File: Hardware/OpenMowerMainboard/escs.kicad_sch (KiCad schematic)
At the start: 3 parts, among them U4 xESC2, U5 xESC2, U6 xESC2

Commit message: wip schematic
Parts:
- added D10, D11, D12, D4, D5, D6, D7, D8, D9: D_TVS, Diode_SMD:D_SMB, symbol Device:D_TVS
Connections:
- net MC_HALL_U: now also D7.2 (A2), D9.2 (A2)
- net MC_HALL_V: now also D7.1 (A1), D8.2 (A2)
- net MC_HALL_W: now also D8.1 (A1), D9.1 (A1)
- net ML_HALL_U: now also D4.2 (A2), D6.2 (A2)
- net ML_HALL_V: now also D4.1 (A1), D5.2 (A2)
- net ML_HALL_W: now also D5.1 (A1), D6.1 (A1)
- net MR_HALL_U: now also D10.2 (A2), D12.2 (A2)
- net MR_HALL_V: now also D10.1 (A1), D11.2 (A2)
- net MR_HALL_W: now also D11.1 (A1), D12.1 (A1)

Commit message: wip
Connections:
- net MC_HALL_U: no longer D7.2 (A2), D9.2 (A2)
- net MC_HALL_V: no longer D7.1 (A1), D8.2 (A2)
- net MC_HALL_W: no longer D8.1 (A1), D9.1 (A1)
- net MC_PHASE_U: now also D7.2 (A2), D9.2 (A2)
- net MC_PHASE_V: now also D7.1 (A1), D8.2 (A2)
- net MC_PHASE_W: now also D8.1 (A1), D9.1 (A1)
- net ML_HALL_U: no longer D4.2 (A2), D6.2 (A2)
- net ML_HALL_V: no longer D4.1 (A1), D5.2 (A2)
- net ML_HALL_W: no longer D5.1 (A1), D6.1 (A1)
- net ML_PHASE_U: now also D4.2 (A2), D6.2 (A2)
- net ML_PHASE_V: now also D4.1 (A1), D5.2 (A2)
- net ML_PHASE_W: now also D5.1 (A1), D6.1 (A1)
- net MR_HALL_U: no longer D10.2 (A2), D12.2 (A2)
- net MR_HALL_V: no longer D10.1 (A1), D11.2 (A2)
- net MR_HALL_W: no longer D11.1 (A1), D12.1 (A1)
- net MR_PHASE_U: now also D10.2 (A2), D12.2 (A2)
- net MR_PHASE_V: now also D10.1 (A1), D11.2 (A2)
- net MR_PHASE_W: now also D11.1 (A1), D12.1 (A1)
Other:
- moved on the sheet: D10, D11, D12, D4, D5, D6, D7, D8, D9

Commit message: wip pcb layout
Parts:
- added C2, C3, C4, C6, C7, C8: C_Polarized, Capacitor_THT:CP_Radial_D10.0mm_P5.00mm, symbol Device:C_Polarized
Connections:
- net GND: now also C2.2, C3.2, C4.2, C6.2, C7.2, C8.2
- net MOSFET_SWITCH/VOUT: now also C2.1, C6.1
- net MOSFET_SWITCH1/VOUT: now also C4.1, C8.1
- net MOSFET_SWITCH2/VOUT: now also C3.1, C7.1

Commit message: WIP hardware revision
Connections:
- net MOSFET_SWITCH/VOUT is gone; now on net V_BATT: C2.1, C6.1, U4.VM (VIN)
- net MOSFET_SWITCH1/VOUT is gone; now on net V_BATT: C4.1, C8.1, U6.VM (VIN)
- net MOSFET_SWITCH2/VOUT is gone; now on net V_BATT: C3.1, C7.1, U5.VM (VIN)
- now unconnected: U4.1 (CAN_L), U4.2 (CAN_H), U5.1 (CAN_L), U5.2 (CAN_H), U6.1 (CAN_L), U6.2 (CAN_H)
- no-connect marks 20 -> 26
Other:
- removed sheet MOSFET_SWITCH
- removed sheet MOSFET_SWITCH1
- removed sheet MOSFET_SWITCH2

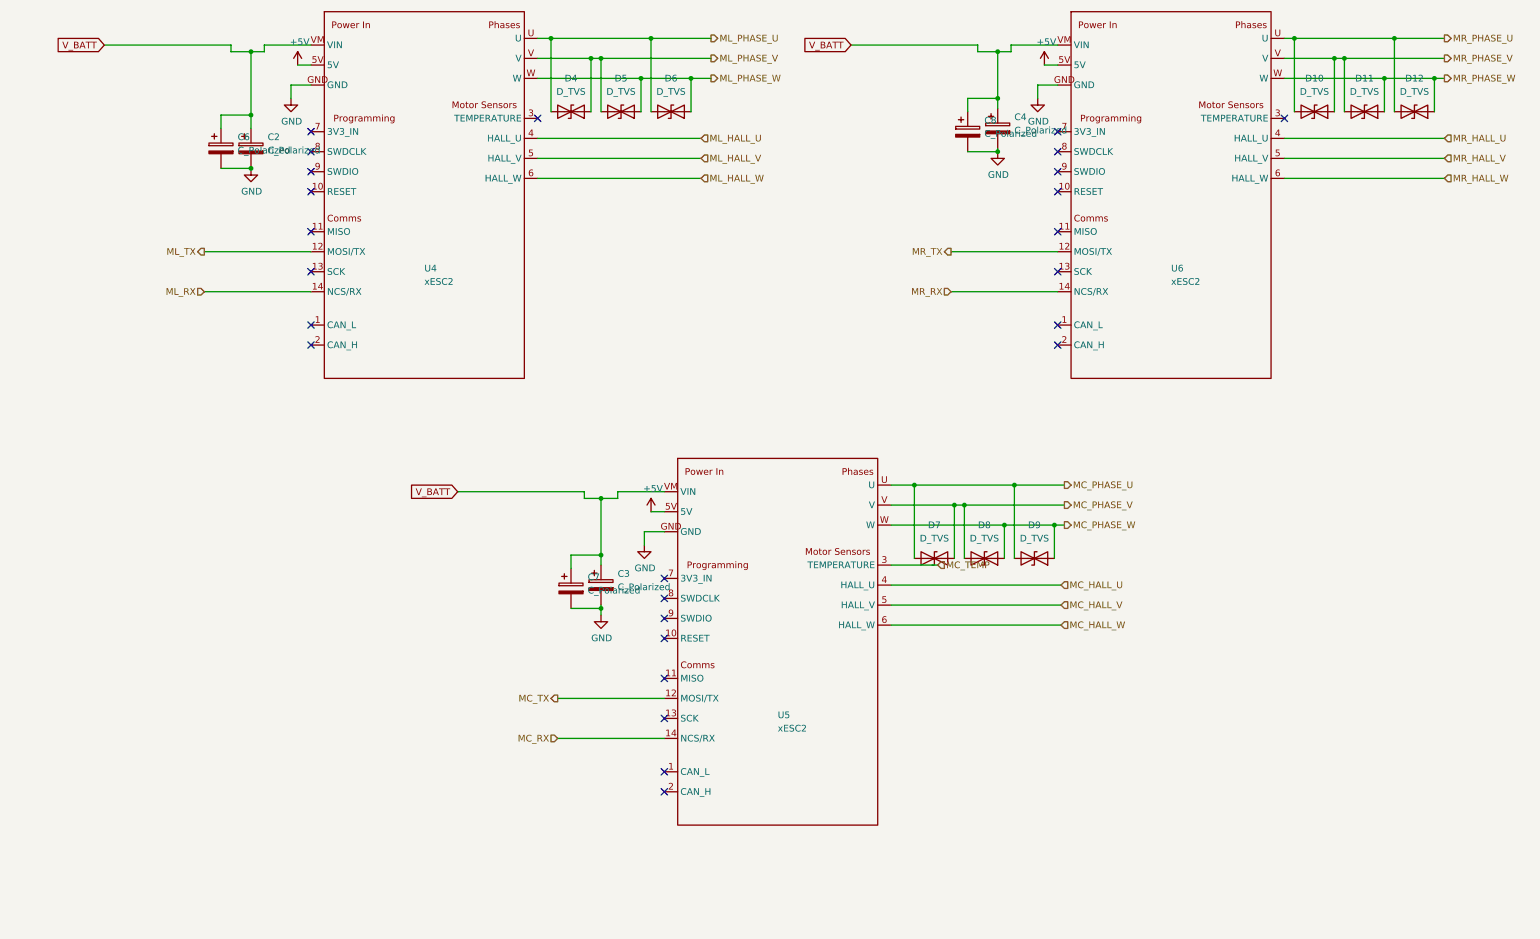
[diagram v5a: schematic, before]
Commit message: v0_9_1 mainboard rework
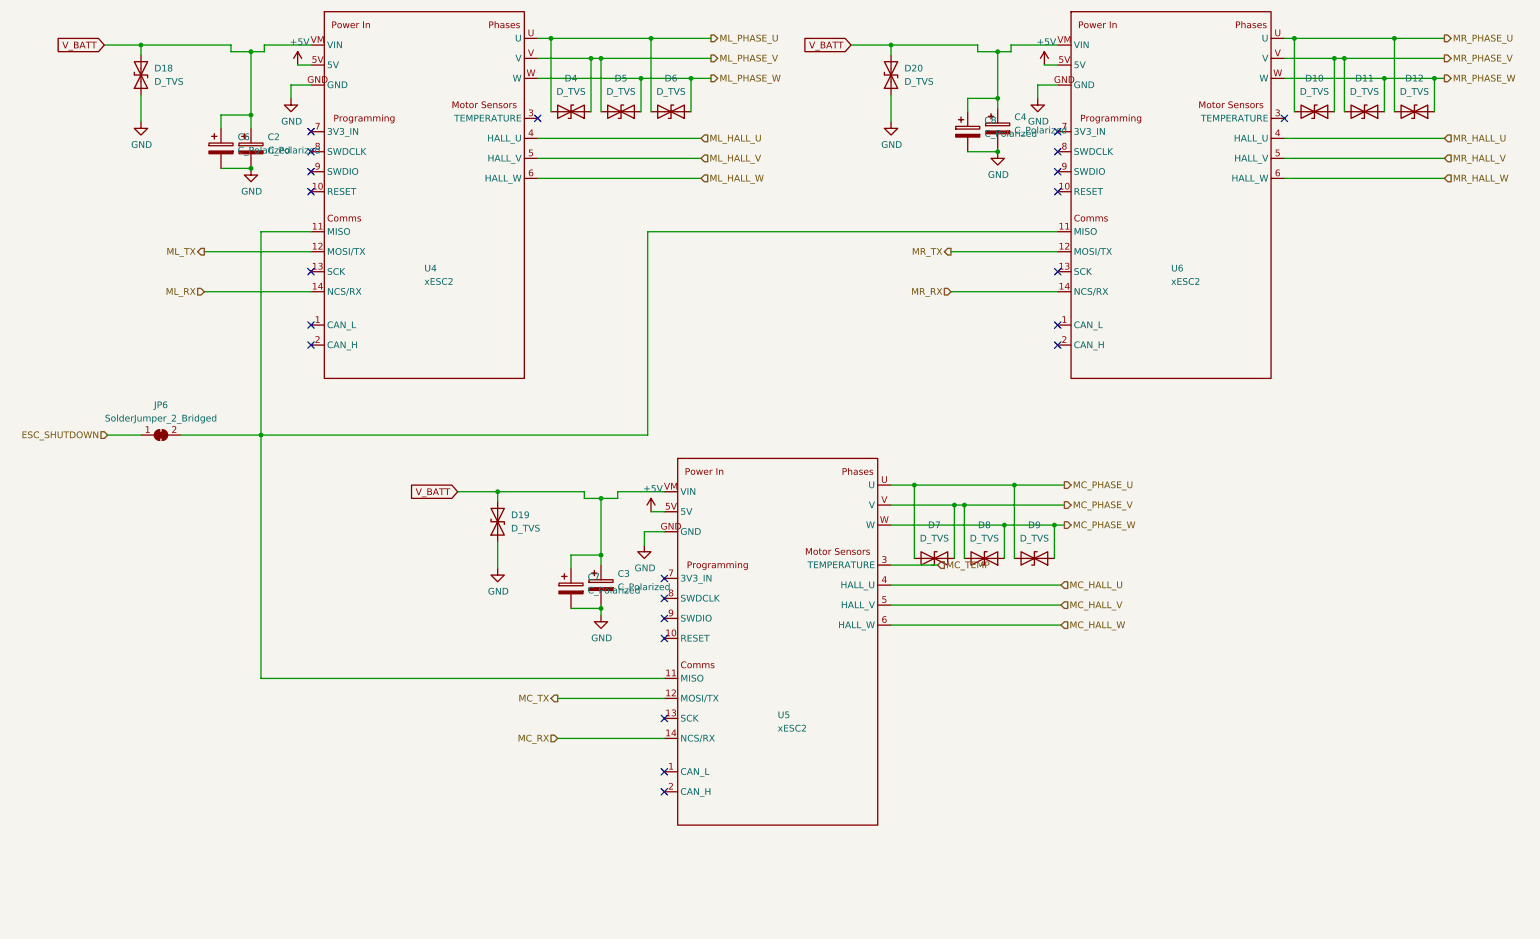
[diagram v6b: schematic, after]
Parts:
- added D18, D19, D20: D_TVS, Diode_SMD:D_SMA, symbol Device:D_TVS
- added JP6: SolderJumper_2_Bridged, Jumper:SolderJumper-2_P1.3mm_Bridged_RoundedPad1.0x1.5mm, symbol Jumper:SolderJumper_2_Bridged
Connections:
- net GND: now also D18.1 (A1), D19.1 (A1), D20.1 (A1)
- net V_BATT: now also D18.2 (A2), D19.2 (A2), D20.2 (A2)
- net at U6.11 (MISO): now also U4.11 (MISO), U5.11 (MISO), JP6.2 (B)
- new net ESC_SHUTDOWN: JP6.1 (A)
- no-connect marks 26 -> 23

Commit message: added some valued, exported iBOM
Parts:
- D10, D11, D12, D18, D19, D20, D4, D5, D6, D7, D8, D9: value D_TVS -> DNP
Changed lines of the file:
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@@
     (in_bom yes) (on_board yes) (fields_autoplaced)
     (property "Reference" "D11" (id 0) (at 265.43 31.75 0))
-    (property "Value" "D_TVS" (id 1) (at 265.43 34.29 0))
+    (property "Value" "DNP" (id 1) (at 265.43 34.29 0))
     (property "Footprint" "Diode_SMD:D_SMB" (id 2) (at 265.43 38.1 0)
       (effects (font (size 1.27 1.27)) hide)
@@
       (effects (font (size 1.27 1.27)) (justify right))
     )
-    (property "Value" "D_TVS" (id 1) (at 102.87 117.4749 90)
+    (property "Value" "DNP" (id 1) (at 102.87 117.4749 90)
       (effects (font (size 1.27 1.27)) (justify right))
     )
@@
     (in_bom yes) (on_board yes) (fields_autoplaced)
     (property "Reference" "D10" (id 0) (at 255.905 31.75 0))
-    (property "Value" "D_TVS" (id 1) (at 255.905 34.29 0))
+    (property "Value" "DNP" (id 1) (at 255.905 34.29 0))
     (property "Footprint" "Diode_SMD:D_SMB" (id 2) (at 255.905 38.1 0)
       (effects (font (size 1.27 1.27)) hide)
@@
     (in_bom yes) (on_board yes) (fields_autoplaced)
     (property "Reference" "D6" (id 0) (at 133.35 31.75 0))
-    (property "Value" "D_TVS" (id 1) (at 133.35 34.29 0))
+    (property "Value" "DNP" (id 1) (at 133.35 34.29 0))
     (property "Footprint" "Diode_SMD:D_SMB" (id 2) (at 133.35 38.1 0)
       (effects (font (size 1.27 1.27)) hide)
@@
     (in_bom yes) (on_board yes) (fields_autoplaced)
     (property "Reference" "D4" (id 0) (at 114.3 31.75 0))
-    (property "Value" "D_TVS" (id 1) (at 114.3 34.29 0))
+    (property "Value" "DNP" (id 1) (at 114.3 34.29 0))
     (property "Footprint" "Diode_SMD:D_SMB" (id 2) (at 114.3 38.1 0)
       (effects (font (size 1.27 1.27)) hide)
@@
     (in_bom yes) (on_board yes) (fields_autoplaced)
     (property "Reference" "D5" (id 0) (at 123.825 31.75 0))
-    (property "Value" "D_TVS" (id 1) (at 123.825 34.29 0))
+    (property "Value" "DNP" (id 1) (at 123.825 34.29 0))
     (property "Footprint" "Diode_SMD:D_SMB" (id 2) (at 123.825 38.1 0)
       (effects (font (size 1.27 1.27)) hide)
@@
     (in_bom yes) (on_board yes) (fields_autoplaced)
     (property "Reference" "D7" (id 0) (at 183.515 116.84 0))
-    (property "Value" "D_TVS" (id 1) (at 183.515 119.38 0))
+    (property "Value" "DNP" (id 1) (at 183.515 119.38 0))
     (property "Footprint" "Diode_SMD:D_SMB" (id 2) (at 183.515 123.19 0)
       (effects (font (size 1.27 1.27)) hide)
@@
     (in_bom yes) (on_board yes) (fields_autoplaced)
     (property "Reference" "D9" (id 0) (at 202.565 116.84 0))
-    (property "Value" "D_TVS" (id 1) (at 202.565 119.38 0))
+    (property "Value" "DNP" (id 1) (at 202.565 119.38 0))
     (property "Footprint" "Diode_SMD:D_SMB" (id 2) (at 202.565 123.19 0)
       (effects (font (size 1.27 1.27)) hide)
@@
     (in_bom yes) (on_board yes) (fields_autoplaced)
     (property "Reference" "D12" (id 0) (at 274.955 31.75 0))
-    (property "Value" "D_TVS" (id 1) (at 274.955 34.29 0))
+    (property "Value" "DNP" (id 1) (at 274.955 34.29 0))
     (property "Footprint" "Diode_SMD:D_SMB" (id 2) (at 274.955 38.1 0)
       (effects (font (size 1.27 1.27)) hide)
@@
       (effects (font (size 1.27 1.27)) (justify right))
     )
-    (property "Value" "D_TVS" (id 1) (at 177.8 32.3849 90)
+    (property "Value" "DNP" (id 1) (at 177.8 32.3849 90)
       (effects (font (size 1.27 1.27)) (justify right))
     )
@@
       (effects (font (size 1.27 1.27)) (justify right))
     )
-    (property "Value" "D_TVS" (id 1) (at 34.925 32.3849 90)
+    (property "Value" "DNP" (id 1) (at 34.925 32.3849 90)
       (effects (font (size 1.27 1.27)) (justify right))
     )
@@
     (in_bom yes) (on_board yes) (fields_autoplaced)
     (property "Reference" "D8" (id 0) (at 193.04 116.84 0))
-    (property "Value" "D_TVS" (id 1) (at 193.04 119.38 0))
+    (property "Value" "DNP" (id 1) (at 193.04 119.38 0))
     (property "Footprint" "Diode_SMD:D_SMB" (id 2) (at 193.04 123.19 0)
       (effects (font (size 1.27 1.27)) hide)

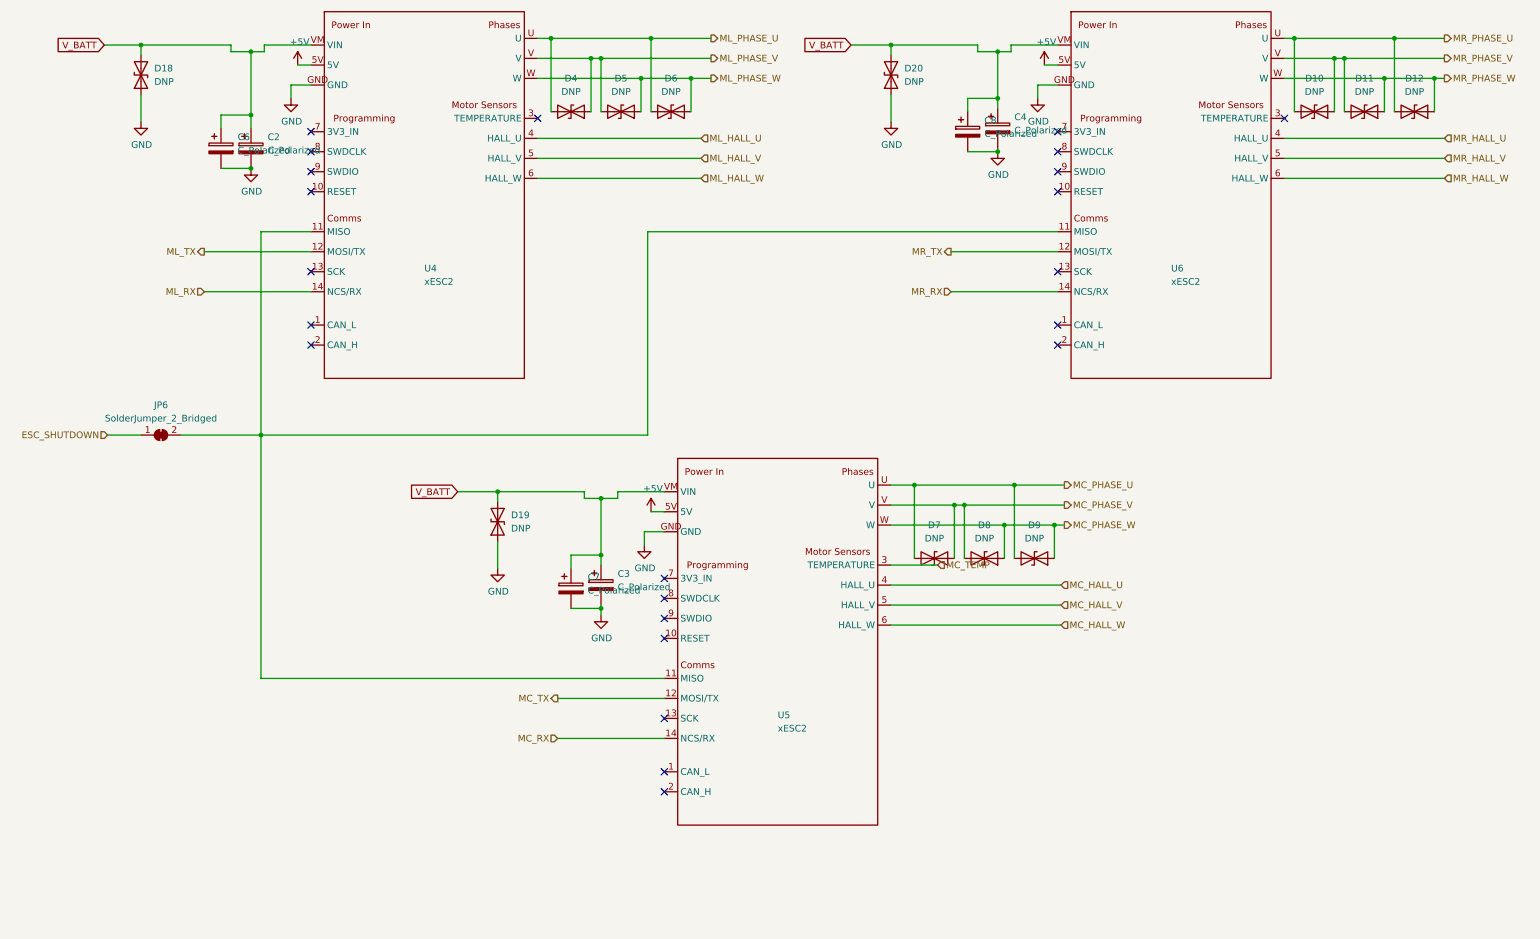
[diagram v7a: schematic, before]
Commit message: BoM data added to kicad - results exported to .xlsx file
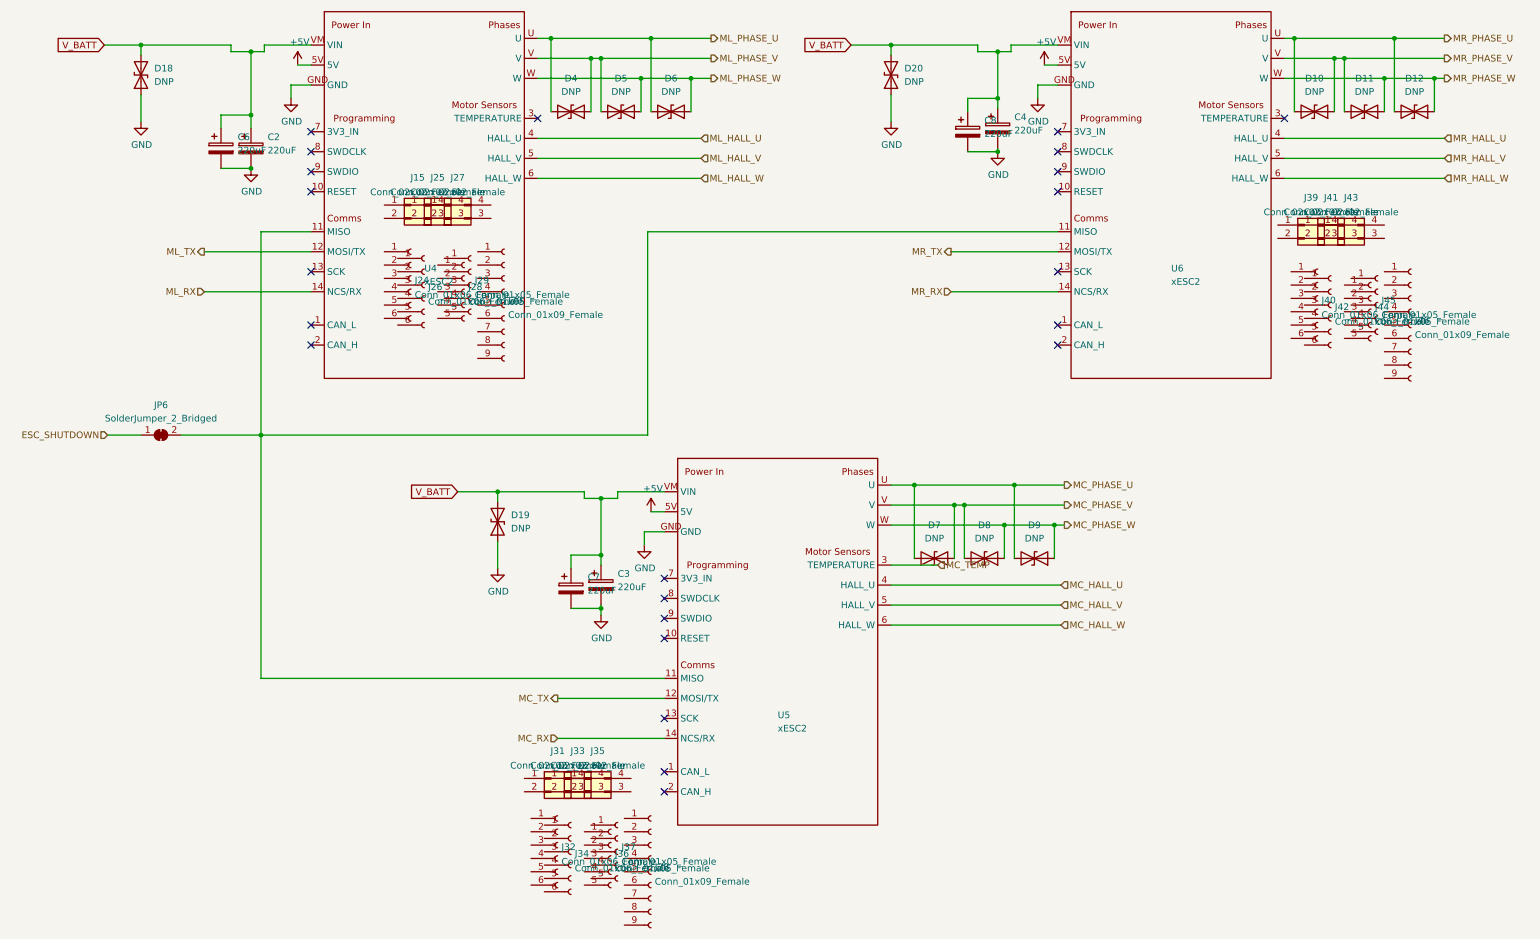
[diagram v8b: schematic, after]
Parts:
- added J15, J25, J27, J31, J33, J35, J39, J41, J43: Conn_02x02_Female, symbol Connector_Generic:Conn_02x02_Counter_Clockwise
- added J24, J26, J32, J34, J40, J42: Conn_01x06_Female, symbol Connector:Conn_01x06_Female
- added J28, J29, J36, J37, J44, J45: Conn_01x05_Female, symbol Connector:Conn_01x05_Female
- added J30, J38, J46: Conn_01x09_Female, symbol Connector:Conn_01x09_Female
- C2, C3, C4, C6, C7, C8: value C_Polarized -> 220uF; LCSC (none) -> C442941; Part Number (none) -> LKME1251J221MF; Stock_PN (none) -> CP-TH-220uF-63V
- D10, D11, D12, D18, D19, D20, D4, D5, D6, D7, D8, D9, JP6, U4, U5, U6: Config (none) -> do not place
